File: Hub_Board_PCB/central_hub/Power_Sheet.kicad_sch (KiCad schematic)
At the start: 19 parts, among them J8 Conn_01x02, U5 AP2112K-3.3TRG1, U7 AP63205WU-7

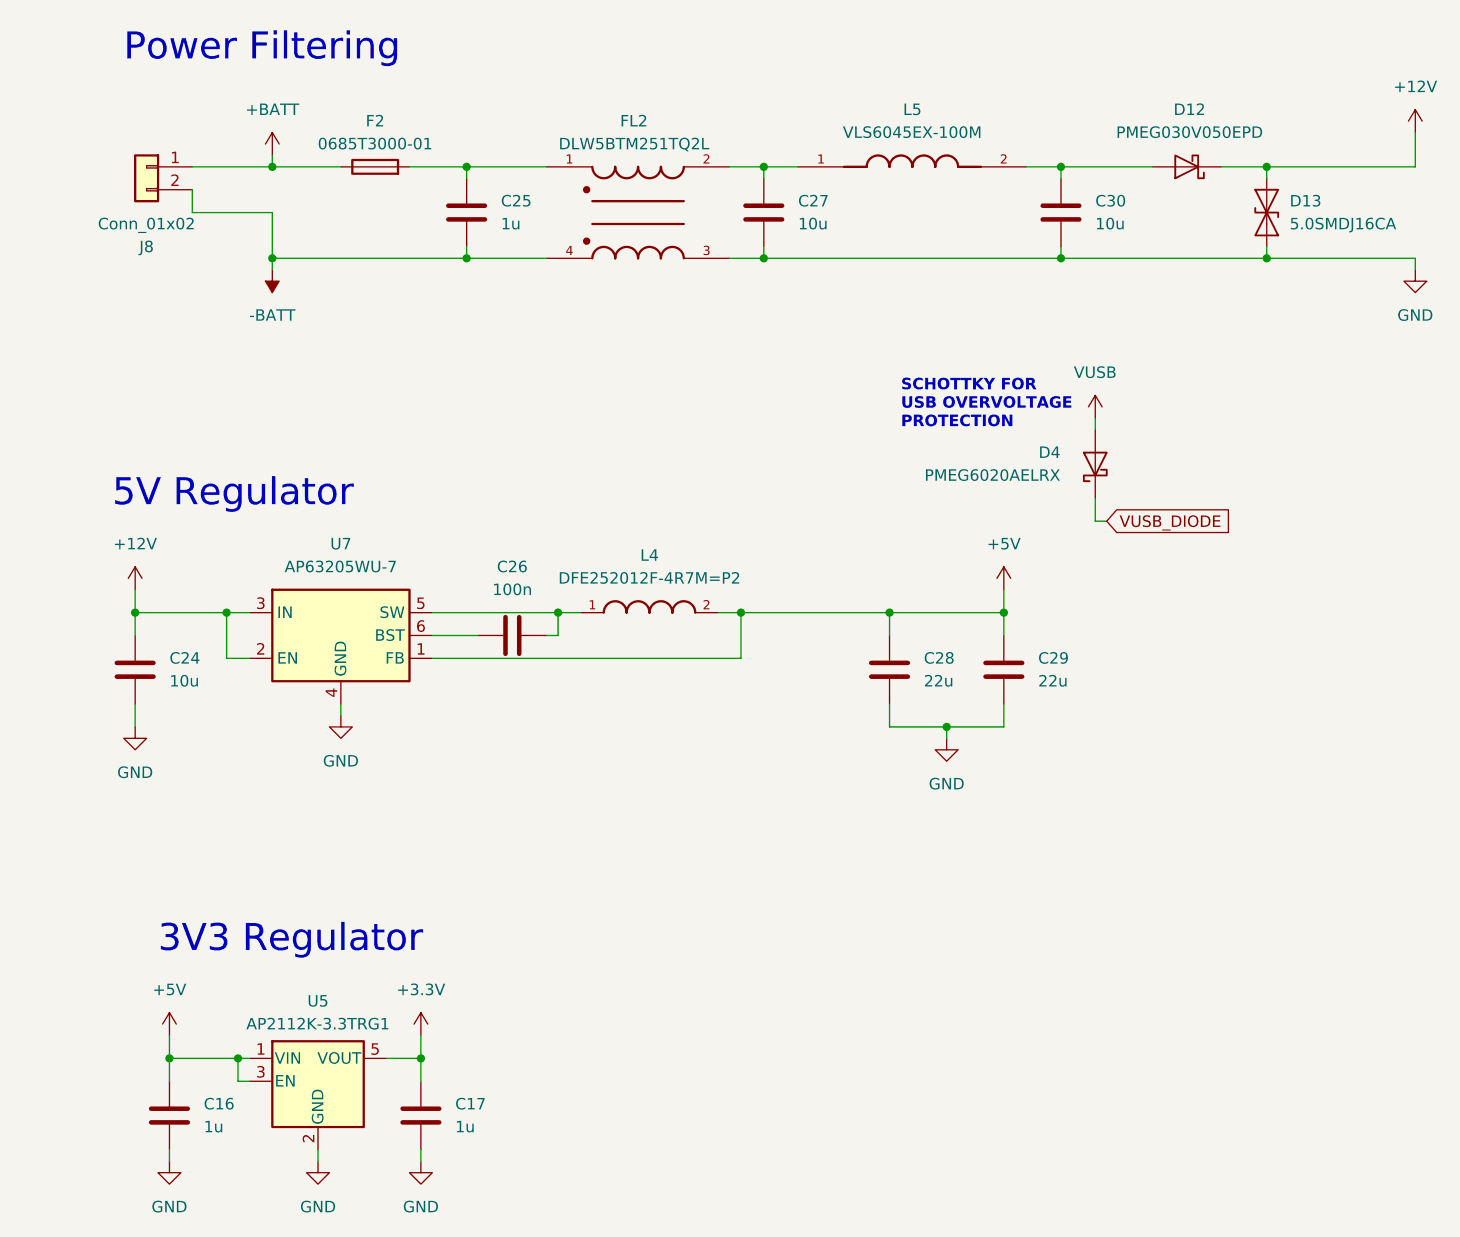
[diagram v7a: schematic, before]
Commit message: - added footprint labels to schematic
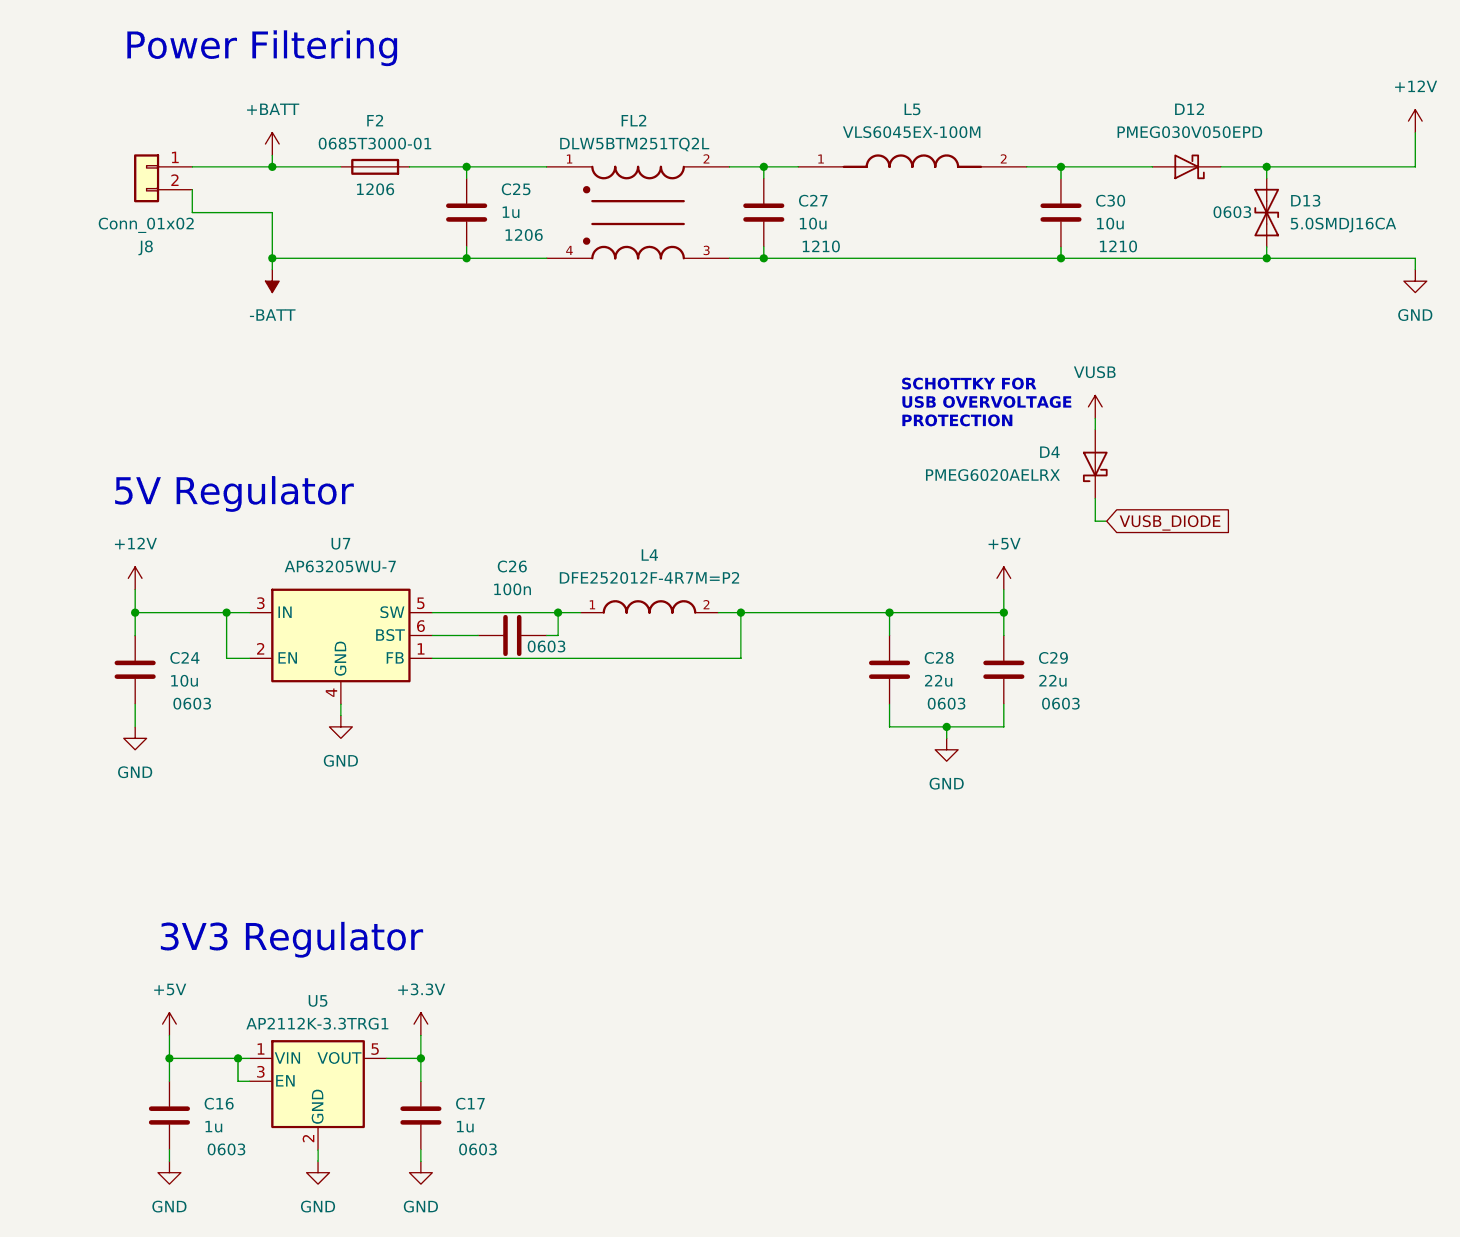
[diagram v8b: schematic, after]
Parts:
- C16, C17, C24, C26, C28, C29, D13: FP (none) -> 0603
- C25, F2: FP (none) -> 1206
- C27, C30: FP (none) -> 1210
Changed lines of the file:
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@@
   )
   (symbol (lib_id "Device:C") (at 36.83 101.6 180) (unit 1)
-    (in_bom yes) (on_board yes) (dnp no) (fields_autoplaced)
+    (in_bom yes) (on_board yes) (dnp no)
     (property "Reference" "C24" (at 40.64 100.33 0)
       (effects (font (size 1.27 1.27)) (justify right))
@@
     (property "Datasheet" "~" (at 36.83 101.6 0)
       (effects (font (size 1.27 1.27)) hide)
+    )
+    (property "FP" "0603" (at 43.18 105.41 0)
+      (effects (font (size 1.27 1.27)))
     )
     (pin "1")
@@
   )
   (symbol (lib_id "Device:C") (at 120.65 101.6 180) (unit 1)
-    (in_bom yes) (on_board yes) (dnp no) (fields_autoplaced)
+    (in_bom yes) (on_board yes) (dnp no)
     (property "Reference" "C28" (at 124.46 100.33 0)
       (effects (font (size 1.27 1.27)) (justify right))
@@
       (effects (font (size 1.27 1.27)) hide)
     )
+    (property "FP" "0603" (at 127 105.41 0)
+      (effects (font (size 1.27 1.27)))
+    )
     (pin "1")
     (pin "2")
@@
   )
   (symbol (lib_id "Device:C") (at 133.35 101.6 180) (unit 1)
-    (in_bom yes) (on_board yes) (dnp no) (fields_autoplaced)
+    (in_bom yes) (on_board yes) (dnp no)
     (property "Reference" "C29" (at 137.16 100.33 0)
       (effects (font (size 1.27 1.27)) (justify right))
@@
       (effects (font (size 1.27 1.27)) hide)
     )
+    (property "FP" "0603" (at 139.7 105.41 0)
+      (effects (font (size 1.27 1.27)))
+    )
     (pin "1")
     (pin "2")
@@
   )
   (symbol (lib_id "Device:Fuse") (at 63.5 45.72 90) (unit 1)
-    (in_bom yes) (on_board yes) (dnp no) (fields_autoplaced)
+    (in_bom yes) (on_board yes) (dnp no)
     (property "Reference" "F2" (at 63.5 40.64 90)
       (effects (font (size 1.27 1.27)))
@@
     (property "Datasheet" "~" (at 63.5 45.72 0)
       (effects (font (size 1.27 1.27)) hide)
+    )
+    (property "FP" "1206" (at 63.5 48.26 90)
+      (effects (font (size 1.27 1.27)))
     )
     (pin "1")
@@
   )
   (symbol (lib_id "Device:C") (at 106.68 50.8 180) (unit 1)
-    (in_bom yes) (on_board yes) (dnp no) (fields_autoplaced)
+    (in_bom yes) (on_board yes) (dnp no)
     (property "Reference" "C27" (at 110.49 49.53 0)
       (effects (font (size 1.27 1.27)) (justify right))
@@
       (effects (font (size 1.27 1.27)) hide)
     )
+    (property "FP" "1210" (at 113.03 54.61 0)
+      (effects (font (size 1.27 1.27)))
+    )
     (pin "1")
     (pin "2")
@@
   )
   (symbol (lib_id "Device:C") (at 73.66 50.8 180) (unit 1)
-    (in_bom yes) (on_board yes) (dnp no) (fields_autoplaced)
-    (property "Reference" "C25" (at 77.47 49.53 0)
-      (effects (font (size 1.27 1.27)) (justify right))
-    )
-    (property "Value" "1u" (at 77.47 52.07 0)
+    (in_bom yes) (on_board yes) (dnp no)
+    (property "Reference" "C25" (at 77.47 48.26 0)
+      (effects (font (size 1.27 1.27)) (justify right))
+    )
+    (property "Value" "1u" (at 77.47 50.8 0)
       (effects (font (size 1.27 1.27)) (justify right))
     )
@@
       (effects (font (size 1.27 1.27)) hide)
     )
+    (property "FP" "1206" (at 80.01 53.34 0)
+      (effects (font (size 1.27 1.27)))
+    )
     (pin "1")
     (pin "2")
@@
   )
   (symbol (lib_id "Diode:SMAJ18CA") (at 162.56 50.8 90) (unit 1)
-    (in_bom yes) (on_board yes) (dnp no) (fields_autoplaced)
+    (in_bom yes) (on_board yes) (dnp no)
     (property "Reference" "D13" (at 165.1 49.53 90)
       (effects (font (size 1.27 1.27)) (justify right))
@@
       (effects (font (size 1.27 1.27)) hide)
     )
+    (property "FP" "0603" (at 158.75 50.8 90)
+      (effects (font (size 1.27 1.27)))
+    )
     (pin "1")
     (pin "2")
@@
   )
   (symbol (lib_id "Device:C") (at 40.64 151.13 180) (unit 1)
-    (in_bom yes) (on_board yes) (dnp no) (fields_autoplaced)
+    (in_bom yes) (on_board yes) (dnp no)
     (property "Reference" "C16" (at 44.45 149.86 0)
       (effects (font (size 1.27 1.27)) (justify right))
@@
     (property "Datasheet" "~" (at 40.64 151.13 0)
       (effects (font (size 1.27 1.27)) hide)
+    )
+    (property "FP" "0603" (at 46.99 154.94 0)
+      (effects (font (size 1.27 1.27)))
     )
     (pin "1")
@@
   )
   (symbol (lib_id "Device:C") (at 78.74 97.79 90) (unit 1)
-    (in_bom yes) (on_board yes) (dnp no) (fields_autoplaced)
+    (in_bom yes) (on_board yes) (dnp no)
     (property "Reference" "C26" (at 78.74 90.17 90)
       (effects (font (size 1.27 1.27)))
@@
       (effects (font (size 1.27 1.27)) hide)
     )
+    (property "FP" "0603" (at 82.55 99.06 90)
+      (effects (font (size 1.27 1.27)))
+    )
     (pin "1")
     (pin "2")
@@
   )
   (symbol (lib_id "Device:C") (at 139.7 50.8 180) (unit 1)
-    (in_bom yes) (on_board yes) (dnp no) (fields_autoplaced)
+    (in_bom yes) (on_board yes) (dnp no)
     (property "Reference" "C30" (at 143.51 49.53 0)
       (effects (font (size 1.27 1.27)) (justify right))
@@
       (effects (font (size 1.27 1.27)) hide)
     )
+    (property "FP" "1210" (at 146.05 54.61 0)
+      (effects (font (size 1.27 1.27)))
+    )
     (pin "1")
     (pin "2")
@@
   )
   (symbol (lib_id "Device:C") (at 68.58 151.13 180) (unit 1)
-    (in_bom yes) (on_board yes) (dnp no) (fields_autoplaced)
+    (in_bom yes) (on_board yes) (dnp no)
     (property "Reference" "C17" (at 72.39 149.86 0)
       (effects (font (size 1.27 1.27)) (justify right))
@@
       (effects (font (size 1.27 1.27)) hide)
     )
-    (pin "1")
+    (property "FP" "0603" (at 74.93 154.94 0)
+      (effects (font (size 1.27 1.27)))
+    )
+    (pin "1")
